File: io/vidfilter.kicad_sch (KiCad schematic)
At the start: 14 parts

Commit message: External I/O
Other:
- moved on the sheet: C349, C350, C351, C352, D3, D3A, D3B, D4, D4A, D4B, L1, L2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

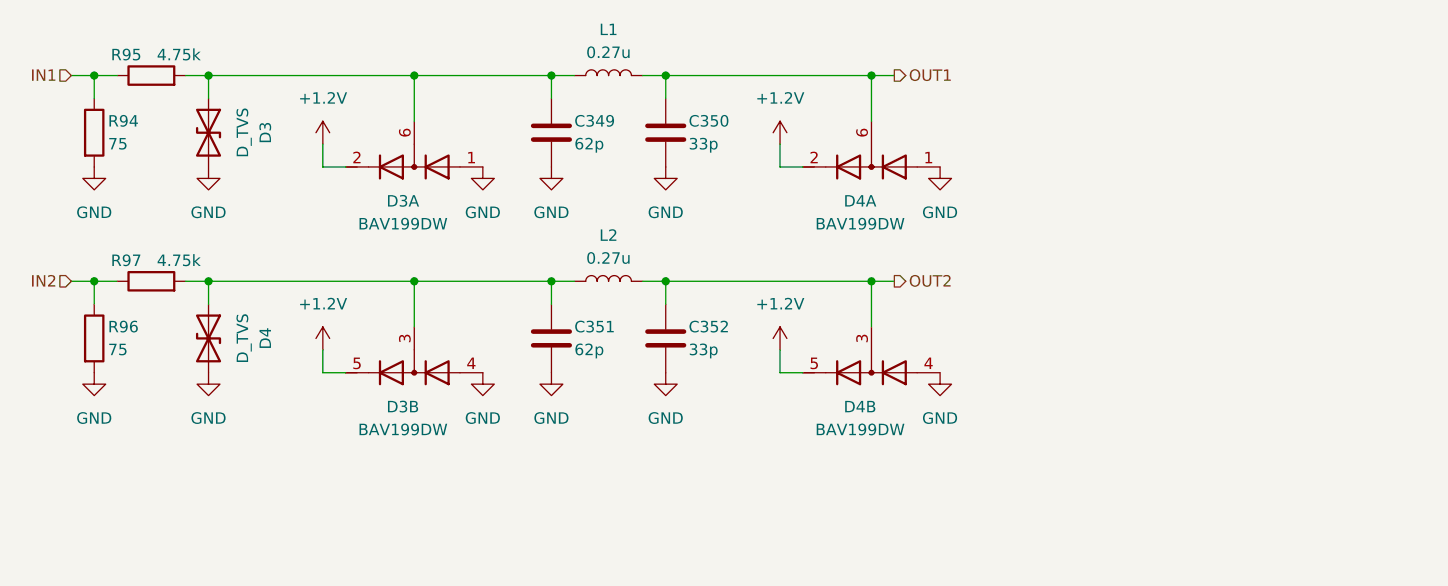
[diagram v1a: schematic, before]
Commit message: Audio Output, Analog isolation and TOSLINK
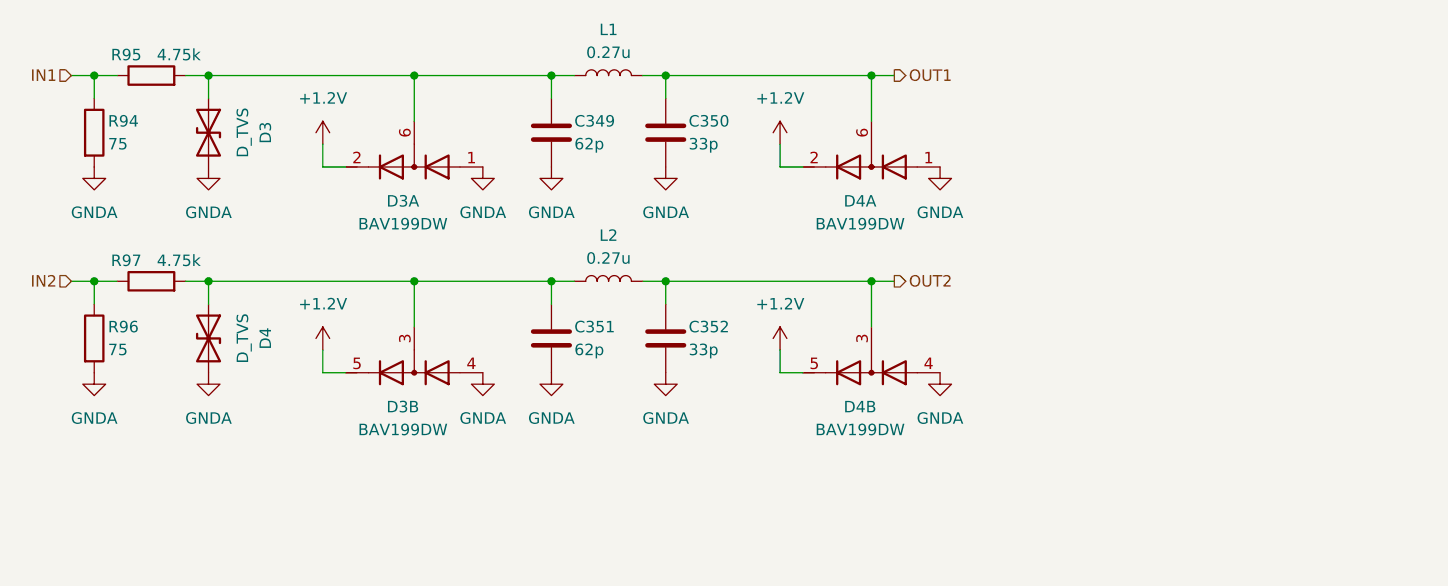
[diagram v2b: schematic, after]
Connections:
- net GND renamed GNDA

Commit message: Multipurpose and standby power rails, Reannotated schematic
Added V_1P2, V_1P8, V_5P0DUAL, V_EFUSE, V_GPUPCIE, V_3P3STBY and V_1P2STBY
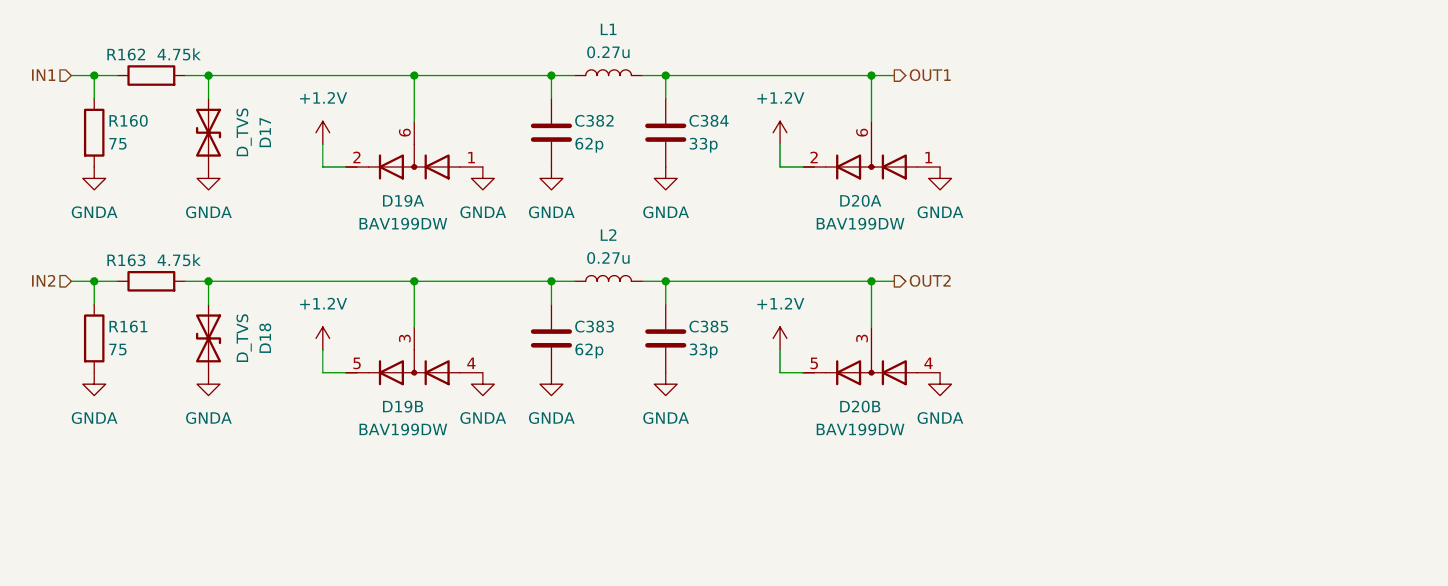
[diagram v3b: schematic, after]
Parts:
- renumbered C349 to C382, C351 to C383, C350 to C384, C352 to C385, D3 to D17, D4 to D18, D3 to D19, D4 to D20, R94 to R160, R96 to R161, R95 to R162, R97 to R163
